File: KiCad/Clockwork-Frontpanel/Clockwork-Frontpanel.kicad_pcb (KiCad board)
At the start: 2 copper layers, 56.4 x 94.2 mm, 15 parts

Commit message: New Gerbers, added the xtal to the BOM, new MH for OLED
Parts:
- D3: value Ext. Imp. (ye) -> Ext. Imp. (or)
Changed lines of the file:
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@@
 			(outputformat 1)
 			(mirror no)
-			(drillshape 1)
+			(drillshape 0)
 			(scaleselection 1)
 			(outputdirectory "")
@@
 		(property ki_fp_filters "MountingHole*")
 		(sheetname "Root")
-		(sheetfile "ImpulsWerk-Frontpanel.kicad_sch")
+		(sheetfile "Clockwork-Frontpanel.kicad_sch")
 		(attr exclude_from_pos_files exclude_from_bom)
 		(fp_circle
@@
 		(property ki_fp_filters "MountingHole*")
 		(sheetname "Root")
-		(sheetfile "ImpulsWerk-Frontpanel.kicad_sch")
+		(sheetfile "Clockwork-Frontpanel.kicad_sch")
 		(attr exclude_from_pos_files exclude_from_bom)
 		(fp_circle
@@
 		(property ki_fp_filters "MountingHole*")
 		(sheetname "Root")
-		(sheetfile "ImpulsWerk-Frontpanel.kicad_sch")
+		(sheetfile "Clockwork-Frontpanel.kicad_sch")
 		(attr exclude_from_pos_files exclude_from_bom)
 		(fp_circle
@@
 		(property ki_fp_filters "MountingHole*")
 		(sheetname "Root")
-		(sheetfile "ImpulsWerk-Frontpanel.kicad_sch")
+		(sheetfile "Clockwork-Frontpanel.kicad_sch")
 		(attr exclude_from_pos_files exclude_from_bom)
 		(fp_circle
@@
 		(property ki_fp_filters "MountingHole*")
 		(sheetname "Root")
-		(sheetfile "ImpulsWerk-Frontpanel.kicad_sch")
+		(sheetfile "Clockwork-Frontpanel.kicad_sch")
 		(attr exclude_from_pos_files exclude_from_bom)
 		(fp_circle
@@
 		(property ki_fp_filters "MountingHole*")
 		(sheetname "Root")
-		(sheetfile "ImpulsWerk-Frontpanel.kicad_sch")
+		(sheetfile "Clockwork-Frontpanel.kicad_sch")
 		(attr exclude_from_pos_files exclude_from_bom)
 		(fp_circle
@@
 		(property ki_fp_filters "MountingHole*")
 		(sheetname "Root")
-		(sheetfile "ImpulsWerk-Frontpanel.kicad_sch")
+		(sheetfile "Clockwork-Frontpanel.kicad_sch")
 		(attr exclude_from_pos_files exclude_from_bom)
 		(fp_circle
@@
 		(property ki_fp_filters "MountingHole*")
 		(sheetname "Root")
-		(sheetfile "ImpulsWerk-Frontpanel.kicad_sch")
+		(sheetfile "Clockwork-Frontpanel.kicad_sch")
 		(attr exclude_from_pos_files exclude_from_bom)
 		(fp_circle
@@
 		(property ki_fp_filters "R_*")
 		(sheetname "Root")
-		(sheetfile "ImpulsWerk-Frontpanel.kicad_sch")
+		(sheetfile "Clockwork-Frontpanel.kicad_sch")
 		(attr smd)
 		(fp_line
@@
 		(at 134.9695 74.4)
 		(property "Reference" "D1"
-			(at 3.4605 0.022 360)
+			(at 3.4605 0.022 180)
 			(layer "B.SilkS")
 			(effects
@@
 		)
 		(property "Value" "no sync (re)"
-			(at 0 -4 360)
+			(at 0 -4 180)
 			(layer "B.Fab")
 			(effects
@@
 		)
 		(property "Footprint" "easyEDA:LED-SMD_L3.2-W1.6-RD-EH-3_kicad"
-			(at 0 0 360)
+			(at 0 0 180)
 			(layer "B.Fab")
 			(hide yes)
@@
 		)
 		(property "Datasheet" ""
-			(at 0 0 360)
+			(at 0 0 180)
 			(layer "B.Fab")
 			(hide yes)
@@
 		)
 		(property "Description" ""
-			(at 0 0 360)
+			(at 0 0 180)
 			(layer "B.Fab")
 			(hide yes)
@@
 		(property ki_fp_filters "LED* LED_SMD:* LED_THT:*")
 		(sheetname "Root")
-		(sheetfile "ImpulsWerk-Frontpanel.kicad_sch")
+		(sheetfile "Clockwork-Frontpanel.kicad_sch")
 		(attr smd)
 		(fp_line
@@
 		)
 		(fp_text user "${REFERENCE}"
-			(at 0 -2.1 360)
-			(layer "B.Fab")
-			(hide yes)
+			(at 0 -2.1 180)
+			(layer "B.Fab")
 			(effects
 				(font
@@
 		(property ki_fp_filters "R_*")
 		(sheetname "Root")
-		(sheetfile "ImpulsWerk-Frontpanel.kicad_sch")
+		(sheetfile "Clockwork-Frontpanel.kicad_sch")
 		(attr smd)
 		(fp_line
@@
 		(at 134.9875 77.8)
 		(property "Reference" "D3"
-			(at 3.4425 0.178 360)
-			(layer "B.SilkS")
-			(effects
-				(font
-					(size 1 1)
-					(thickness 0.15)
-				)
-				(justify mirror)
-			)
-		)
-		(property "Value" "Ext. Imp. (ye)"
-			(at 0 -4 360)
+			(at 3.4425 0.178 0)
+			(layer "B.SilkS")
+			(effects
+				(font
+					(size 1 1)
+					(thickness 0.15)
+				)
+				(justify mirror)
+			)
+		)
+		(property "Value" "Ext. Imp. (or)"
+			(at 0 -4 0)
 			(layer "B.Fab")
 			(effects
@@
 		)
 		(property "Footprint" "easyEDA:LED-SMD_L3.2-W1.6-RD-EH-3_kicad"
-			(at 0 0 360)
-			(layer "B.Fab")
-			(hide yes)
-			(effects
-				(font
-					(size 1.27 1.27)
-					(thickness 0.15)
-				)
-				(justify mirror)
-			)
-		)
-		(property "Datasheet" ""
-			(at 0 0 360)
+			(at 0 0 0)
+			(layer "B.Fab")
+			(hide yes)
+			(effects
+				(font
+					(size 1.27 1.27)
+					(thickness 0.15)
+				)
+				(justify mirror)
+			)
+		)
+		(property "Datasheet" "https://www.mouser.de/datasheet/2/143/evers03120_1-2266815.pdf"
+			(at 0 0 0)
 			(layer "B.Fab")
 			(hide yes)
@@
 		)
 		(property "Description" ""
-			(at 0 0 360)
+			(at 0 0 0)
 			(layer "B.Fab")
 			(hide yes)
@@
 		(property ki_fp_filters "LED* LED_SMD:* LED_THT:*")
 		(sheetname "Root")
-		(sheetfile "ImpulsWerk-Frontpanel.kicad_sch")
+		(sheetfile "Clockwork-Frontpanel.kicad_sch")
 		(attr smd)
 		(fp_line
@@
 		)
 		(fp_text user "${REFERENCE}"
-			(at 0 -2.1 360)
+			(at 0 -2.1 0)
 			(layer "B.Fab")
 			(hide yes)
@@
 		)
 		(sheetname "Root")
-		(sheetfile "ImpulsWerk-Frontpanel.kicad_sch")
+		(sheetfile "Clockwork-Frontpanel.kicad_sch")
 		(attr smd)
 		(fp_line
@@
 		(property ki_fp_filters "R_*")
 		(sheetname "Root")
-		(sheetfile "ImpulsWerk-Frontpanel.kicad_sch")
+		(sheetfile "Clockwork-Frontpanel.kicad_sch")
 		(attr smd)
 		(fp_line
@@
 		(at 134.9695 71)
 		(property "Reference" "D2"
-			(at 3.4605 0.12 360)
+			(at 3.4605 0.12 180)
 			(layer "B.SilkS")
 			(effects
@@
 		)
 		(property "Value" "Crystal (gr)"
-			(at 0 -4 360)
+			(at 0 -4 180)
 			(layer "B.Fab")
 			(effects
@@
 		)
 		(property "Footprint" "easyEDA:LED-SMD_L3.2-W1.6-RD-EH-3_kicad"
-			(at 0 0 360)
+			(at 0 0 180)
 			(layer "B.Fab")
 			(hide yes)
@@
 		)
 		(property "Datasheet" ""
-			(at 0 0 360)
+			(at 0 0 180)
 			(layer "B.Fab")
 			(hide yes)
@@
 		)
 		(property "Description" ""
-			(at 0 0 360)
+			(at 0 0 180)
 			(layer "B.Fab")
 			(hide yes)
@@
 		(property ki_fp_filters "LED* LED_SMD:* LED_THT:*")
 		(sheetname "Root")
-		(sheetfile "ImpulsWerk-Frontpanel.kicad_sch")
+		(sheetfile "Clockwork-Frontpanel.kicad_sch")
 		(attr smd)
 		(fp_line
@@
 		)
 		(fp_text user "${REFERENCE}"
-			(at 0 -2.1 360)
-			(layer "B.Fab")
-			(hide yes)
-			(effects
-				(font
+			(at 0 -2.1 180)
+			(layer "B.Fab")
+			(effects
+				(font

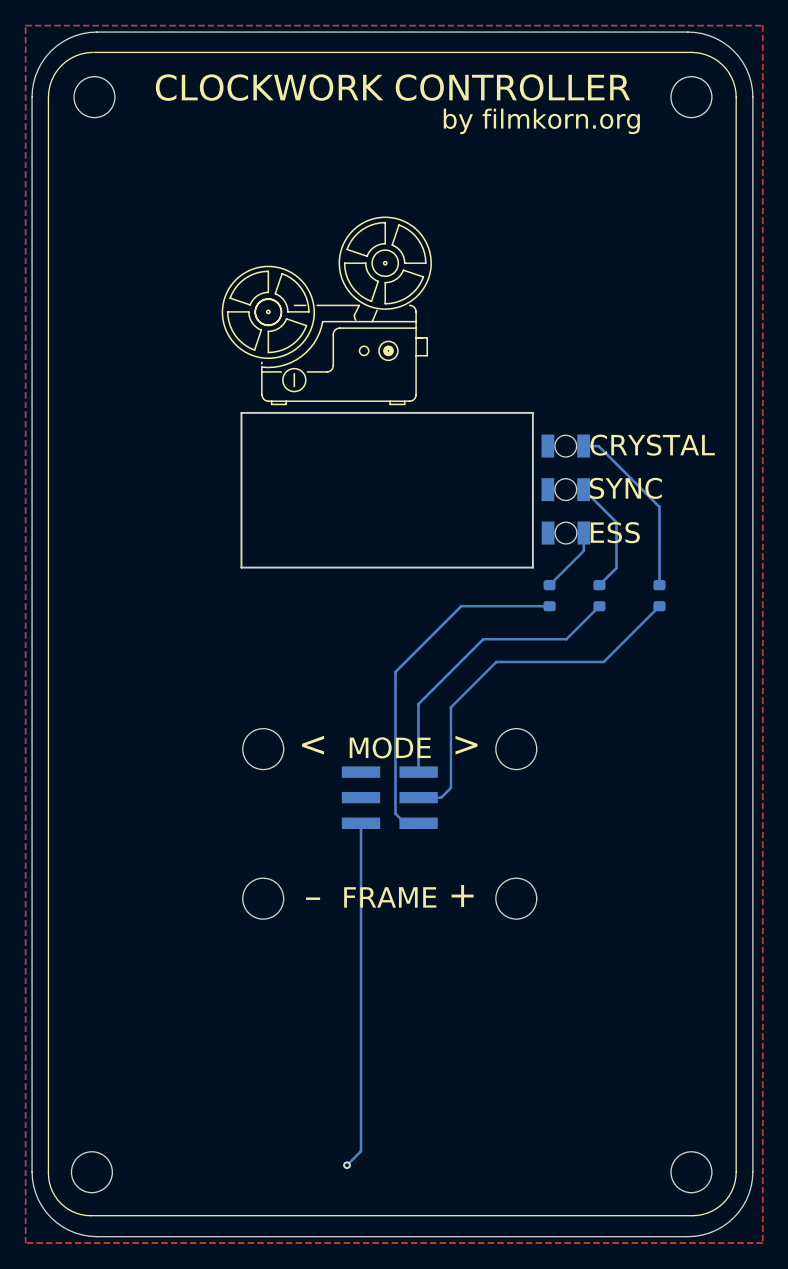
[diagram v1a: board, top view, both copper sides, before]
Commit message: Fixing the Pin Numbering Mess for the Frontpanel LEDs, also, polarity of ESS in LED
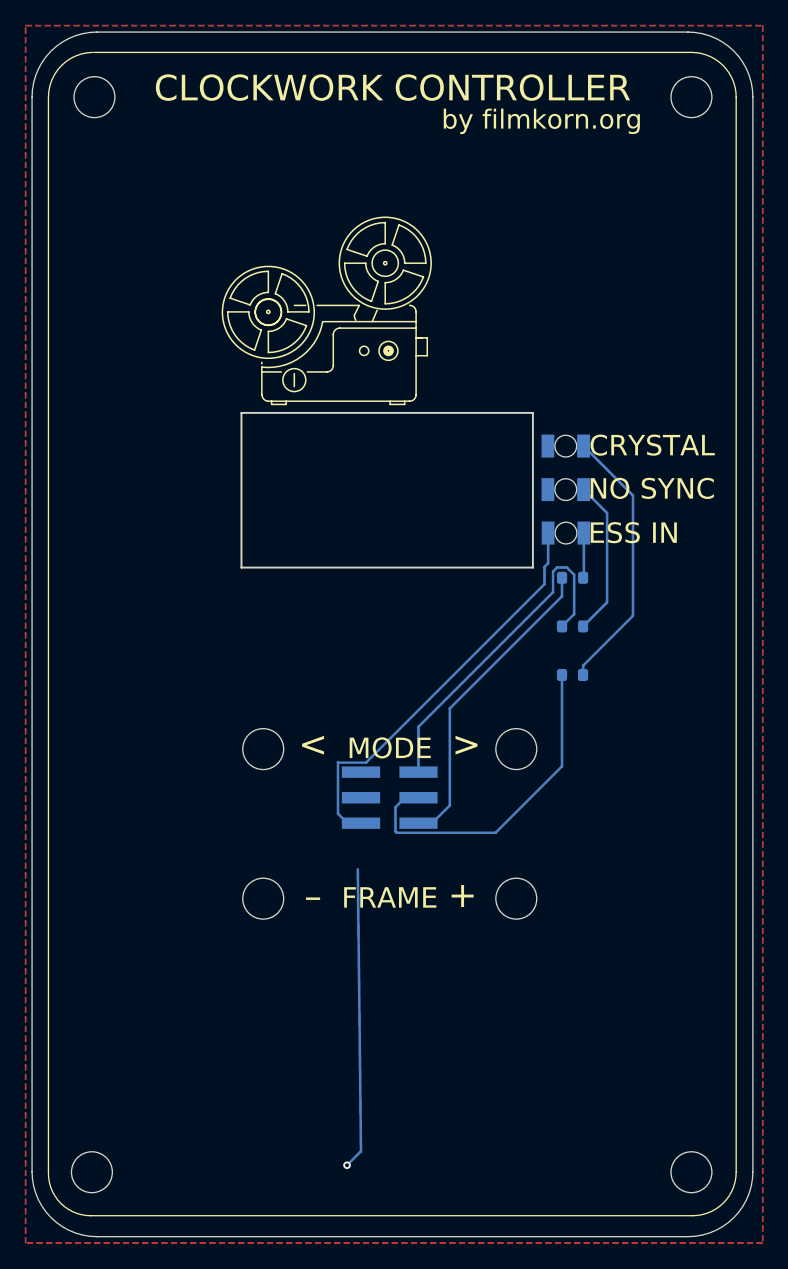
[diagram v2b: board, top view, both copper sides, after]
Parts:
- J1: footprint easyEDA:HDR-SMD_6P-P2.00-V-M-R2-C3-LS6.5 -> easyEDA:HDR-SMD_6P-P2.00-V-M-R2-C3-LS6.5_flipped
- R1: value 3K3 -> 4k7
- R3: value 1k -> 100
- moved R2 9.20 mm to (135.5, 88.9), turned to 0 degrees
- moved R1 3.19 mm to (135.5, 85.1), turned to 0 degrees
- moved R3 2.28 mm to (135.5, 81.3), turned to 180 degrees
- turned D3 to 180 degrees
- turned J1 to 90 degrees
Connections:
- net Net-(J1-Pad3) renamed /Crystal
- D3 pad 1: GND -> Net-(D3-K)
- D3 pad 2: Net-(D3-A) -> /5V
- J1 pad 1: Net-(J1-Pad1) -> /Ext. Imp
- J1 pad 2: GND -> /5V
- J1 pad 5: Net-(J1-Pad5) -> /no Sync
- R1 pad 1: Net-(J1-Pad1) -> /no Sync
- R3 pad 1: Net-(D3-A) -> Net-(D3-K)
- R3 pad 2: Net-(J1-Pad5) -> /Ext. Imp
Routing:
- net /5V: track 0.00 -> 32.2 mm
- net Net-(J1-Pad5): track 27.4 -> 0.00 mm
- net /no Sync: track 0.00 -> 26.5 mm
- net /Ext. Imp: track 0.00 -> 25.5 mm
- net Net-(J1-Pad1): track 22.6 -> 0.00 mm
- net Net-(D2-A): track 14.0 -> 21.1 mm
- net Net-(D3-A): track 5.35 -> 0.00 mm
- net GND: track 28.0 -> 24.4 mm
- net Net-(D3-K): track 0.00 -> 3.53 mm
- net Net-(D1-A): track 9.09 -> 12.2 mm
- net /Crystal: track 28.7 -> 26.4 mm
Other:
- board text added: "ESS IN"
- board text added: "NO SYNC"
- board text removed: "ESS"
- board text removed: "SYNC"

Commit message: Enable Rev.B also for the Forntpanel
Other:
- board text added: "Rev.B"
- board text removed: "Rev.A"
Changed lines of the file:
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@@
 		(layer "Edge.Cuts")
 	)
-	(gr_text "Rev.A"
+	(gr_text "Rev.B"
 		(at 121.2 85.92 0)
 		(layer "B.SilkS")

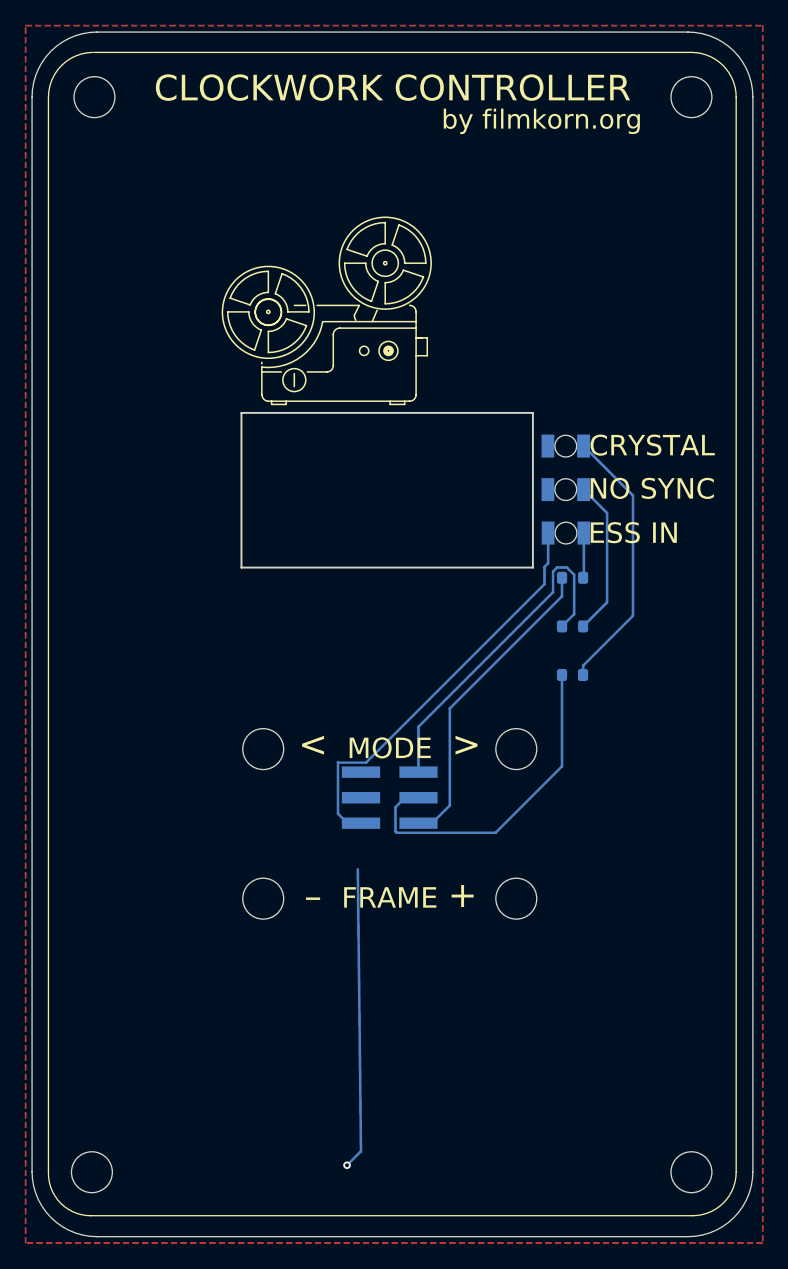
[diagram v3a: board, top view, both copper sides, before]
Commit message: Updated Resistor Values, Button Holes 0.3mm bigger, Display Rect 1mm lower, new LED Labels, Moved GND Via
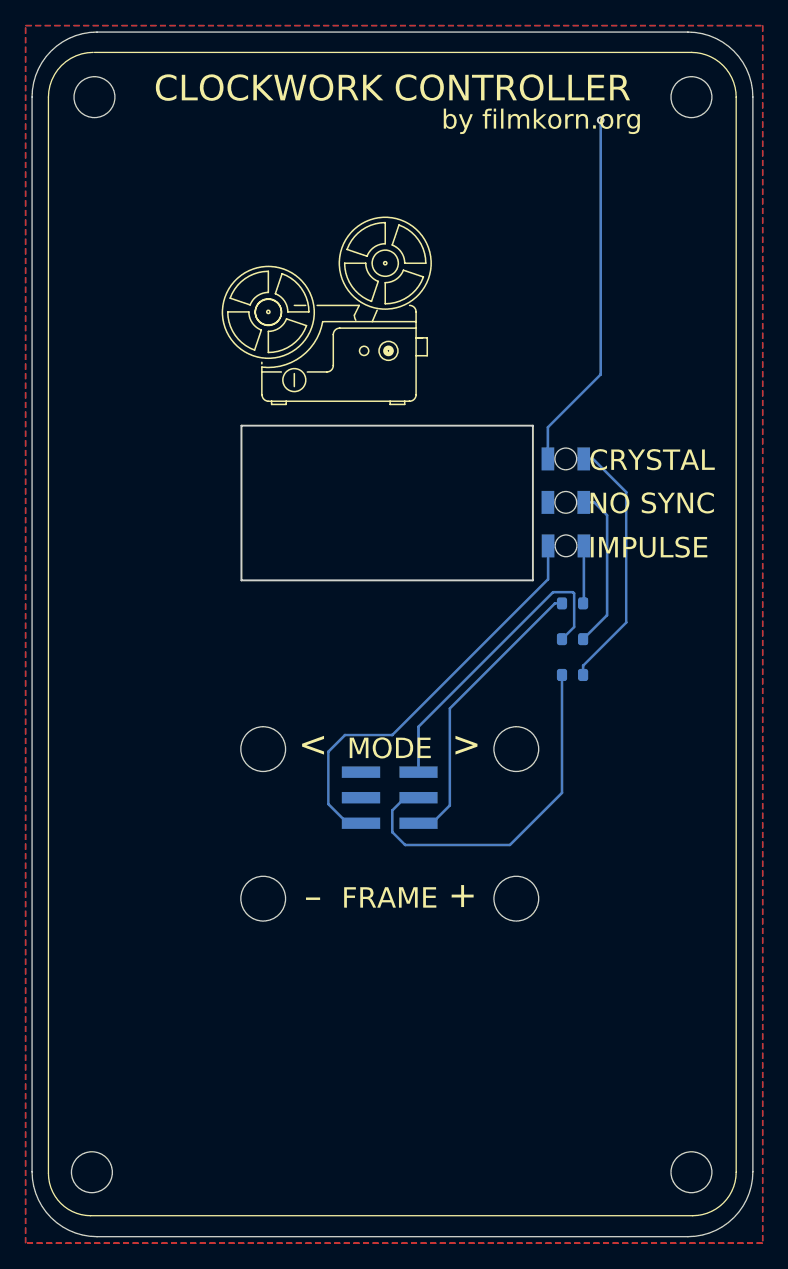
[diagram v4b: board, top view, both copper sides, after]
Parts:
- H5, H6, H7, H8: footprint MountingHole:MountingHole_3.2mm_M3_DIN965 -> Peacemans Teile:MountingHole_3.5mm_M3
- moved R3 2.00 mm to (135.5, 83.3)
- moved D1 1.00 mm to (135.0, 75.4)
- moved D2 1.00 mm to (135.0, 72.0)
- moved D3 1.00 mm to (135.0, 78.8)
- moved R1 1.00 mm to (135.5, 86.1)
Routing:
- net GND: track 24.4 -> 28.2 mm
- net /no Sync: track 26.5 -> 24.1 mm
- net /Crystal: track 26.4 -> 28.8 mm
- net /Ext. Imp: track 25.5 -> 23.8 mm
- net Net-(D2-A): track 21.1 -> 20.1 mm
- net Net-(D3-K): track 3.53 -> 4.53 mm
- net /5V: track 32.2 -> 32.7 mm
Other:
- outline, holes or cut-outs redrawn
- board text added: "IMPULSE"
- board text removed: "ESS IN"
